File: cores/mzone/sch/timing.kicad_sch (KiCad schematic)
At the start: 39 parts

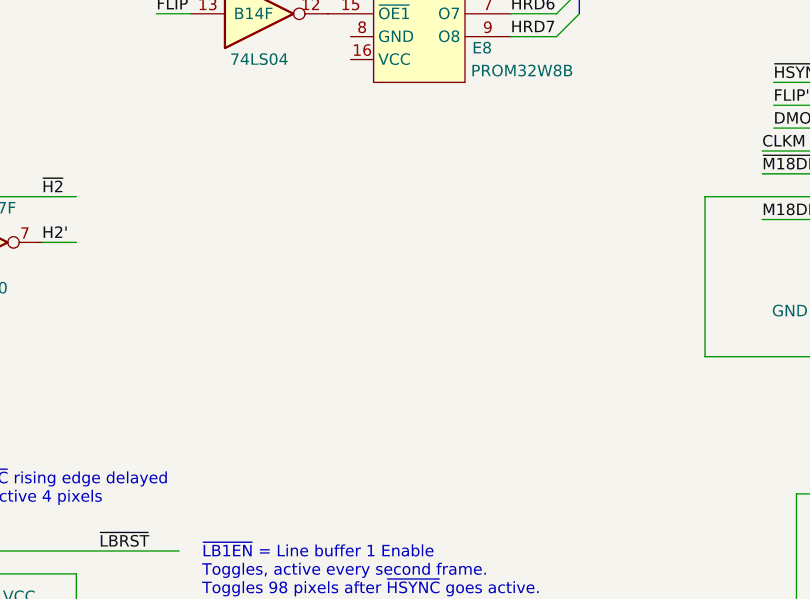
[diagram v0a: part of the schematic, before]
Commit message: mzone core
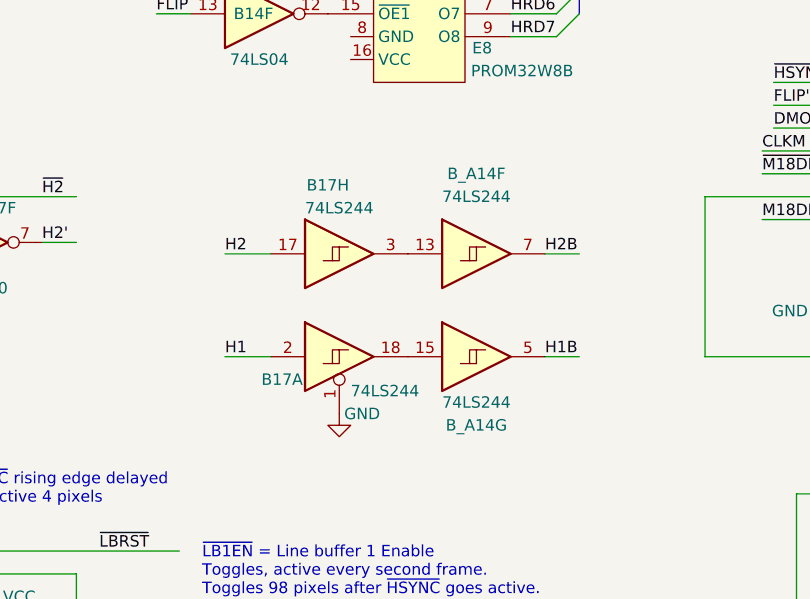
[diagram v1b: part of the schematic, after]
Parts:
- added B17, B_A14: 74LS244, symbol 74xx:74LS244_Split
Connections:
- net GND: now also B17.1
- net H1: now also B17.2
- net H2: now also B17.17
- new net: B17.18, B_A14.15
- new net: B17.3, B_A14.13
- new net H1B: B_A14.5
- new net H2B: B_A14.7

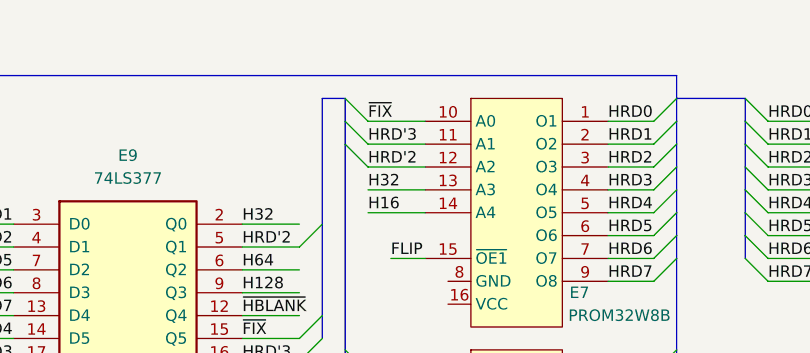
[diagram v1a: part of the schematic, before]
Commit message: mzone core
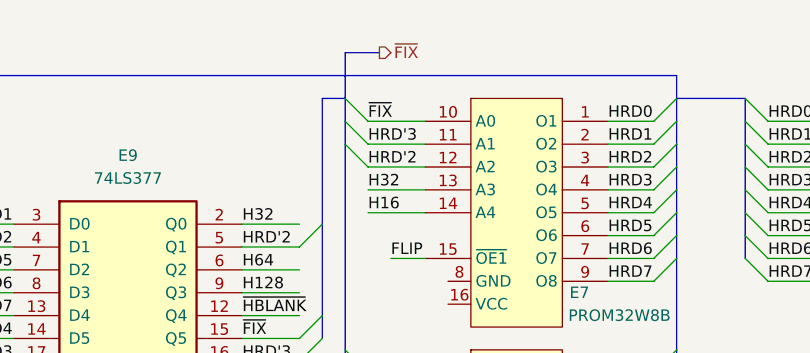
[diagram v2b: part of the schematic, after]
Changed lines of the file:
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@@
 		)
 	)
+	(bus
+		(pts
+			(xy 290.83 22.86) (xy 290.83 17.78)
+		)
+		(stroke
+			(width 0)
+			(type default)
+		)
+	)
 	(wire
 		(pts
@@
 	(bus
 		(pts
+			(xy 290.83 17.78) (xy 294.64 17.78)
+		)
+		(stroke
+			(width 0)
+			(type default)
+		)
+	)
+	(bus
+		(pts
 			(xy 290.83 53.34) (xy 290.83 50.8)
 		)
@@
 	(label "H2"
 		(at 288.29 95.25 0)
-		(fields_autoplaced yes)
 		(effects
 			(font
@@
 	(label "H1B"
 		(at 323.85 106.68 0)
-		(fields_autoplaced yes)
 		(effects
 			(font
@@
 	(label "H2B"
 		(at 323.85 95.25 0)
-		(fields_autoplaced yes)
 		(effects
 			(font
@@
 	(label "H1"
 		(at 288.29 106.68 0)
-		(fields_autoplaced yes)
 		(effects
 			(font
@@
 		(effects
 			(font
+				(size 1.27 1.27)
+			)
+			(justify left)
+		)
+	)
+	(hierarchical_label "~{FIX}"
+		(shape output)
+		(at 294.64 17.78 0)
+		(effects
+			(font

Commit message: mzone core
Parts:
- added unit 7 of G4
- added unit 8 of G4
- added unit 9 of G4
- added unit 3 of G4
- added unit 6 of G4
- added unit 2 of G4
- added unit 4 of G4
- added unit 5 of G4
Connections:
- net GND: now also G4.19
- net ~{M18DIV2}: now also G4.11
- net M18DIV2' renamed ~{OCK}
- net M18DIV4 renamed OC0
- net M18DIV8 renamed OC1
- new net OCK: G4.9
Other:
- note added: "M18DIV16"
- note added: "M18DIV32"
- note added: "M18DIV4"
- note added: "M18DIV8"
- note added: "M18DIV8M4"
- moved on the sheet: G6A

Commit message: mzone core
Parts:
- removed G4: 74LS240, symbol jt74:74LS240
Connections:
- net CLKM is gone; now on net OCK: D7.6
- net CLKM' is gone; now on net OCK': A_D5.3 (I1a)
- net DMOT is gone; now on an unnamed net: A_D14.15 (TC)
- net FLIP': now also G4.4
- net GND: now also G4.1
- net HSYNC76: now also G4.18
- net M18DIV16: now also G4.15
- net OCK: now also G4.8; no longer G4.9
- net ~{DMOT}: now also G4.14
- net ~{FLIP}: now also G4.16
- net ~{HSYNC76}: now also G4.2
- net at C13.1: now also G4.12, G4.13
- net OCK': now reaches G4.7
- net DM0 renamed OA0
- net DM1 renamed OA1
- net DM2 renamed OA2
- net DM3 renamed OA3
- net DM4 renamed OA4
- net DM5 renamed OA5
- net DM6 renamed OA6
- net DM7 renamed OA7
- net OC0 renamed OP0
- net OC1 renamed OP1
- net ~{OCK} renamed ~{OPCK}
- new net OPCK: G4.9
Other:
- note added: "OP1OP0"
- note added: "Object Data Byte"
- note added: "Object Phase counters"
- note removed: "The delay going high is T_LH = 50ohm x 0.47nF = 23.5ns The delay going low is T_HL = 0ns"
- moved on the sheet: A_D14, A_D15, A_D5, B_B14H, B_D14A, C14B, C17H, C40, C43, F6A, F6B, F7A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

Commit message: mzone core
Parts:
- removed E10: 74LS240, symbol jt74:74LS240
- added E10: 74LS240, symbol 74xx:74LS240_Split
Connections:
- net GND: now also B16.2 (GND), E7.8 (GND), E8.8 (GND), G4.10 (GND), E10.1, E10.10 (GND), E10.19; no longer C15.3 (D0), C15.4 (D1), C15.5 (D2), C15.6 (D3)
- net H1: now also E10.11
- net HSYNC: now also E10.12
- net V1: now also B12.9 (~{PE}), B13.9 (~{PE}), B14.2
- net VCC: now also E7.16 (VCC), E8.16 (VCC), G4.20 (VCC), E10.20 (VCC)
- net WRIH: now also E10.5
- net ~{HSYNC}: now also E10.8
- net ~{OP}2: now reaches G4.5
- net CLK1 renamed PXCK1
- net CLK2' renamed PXCK2''
- net DMCNTEN renamed OACNTEN
- net H128 renamed HF128
- net H16 renamed HF16
- net H2F renamed HF2
- net H32 renamed HF32
- net HF32: now also E10.2
- net H4F renamed HF4
- net H64 renamed HF64
- net H8F renamed HF8
- net HSYNC76: no longer names the net of G4.18, G5.2
- net M18: no longer names the net of B16.3 (OUT), C16.12 (C), C16.9 (C), G6.3 (C)
- net M18DIV16 renamed OP2
- net M18DIV32 renamed OP3
- net M18DIV8M4 renamed OP0OP1
- net OCK: no longer names the net of D7.6, G4.8
- net OCK' renamed OACK
- net ~{CLK2} renamed ~{PXCK2}
- net ~{PXCK2}: now also E10.17, E10.4
- net ~{DMCNTEN'} renamed ~{OACNTEN'}
- net ~{DMCNTEN} renamed ~{OACNTEN}
- net ~{DMOT} renamed ~{OAOF}
- net ~{H32}: no longer names the net of B11.1
- net ~{H32}: now also E10.18
- net ~{HSYNC76}: no longer names the net of G2.11 (Q5), G4.2
- net ~{M18DIV2}: no longer names the net of G4.11, G6.5 (Q)
- new net: E10.6, E10.9
- new net: E10.14, E10.15
- new net PXCK2: E10.16
- new net PXCK2': E10.3
- no-connect marks 34 -> 40
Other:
- note added: "Object Counters"
- note added: "Object Line Buffer"
- note added: "PXCK1: f_CLK1 = f_M18 / 3"
- note added: "Pixel clock: 18.432MHz / 3 = 6.144MHz, T = 0.16276us Hsync: Low 32px, High: 352px, Total: 384px, f = 6.144MHz / 384 = 16kHz HBlank: Low 97px (Flipped 96), Front Porch: 32px, Back Porch: 32px, Active pixels: 384 - 97 = 287 (288 flipped)"
- note added: "Vertical Blanking"
- note added: "Vertical Counters"
- note added: "not correct symbol?!"
- note removed: "CLK1: f_CLK1 = f_M18 / 3"
- note removed: "M18DIV16"
- note removed: "M18DIV32"
- note removed: "M18DIV4"
- note removed: "M18DIV8"
- note removed: "M18DIV8M4"
- note removed: "OP1OP0"
- note removed: "Pixel clock: 18.432MHz / 3 = 6.144MHz, T = 0.16276us Hsync: Low 32px, High: 352px, Total: 384px, f = 6.144MHz / 384 = 16kHz HBlank: Low 97px, Front Porch: 32px, Back Porch: 32px, Active pixels: 384 - 97 = 287"
- note removed: "WRIH = H1"
- note removed: "not correct symbol"
- note removed: "not sure GND, check"
- moved on the sheet: A_D14, A_D15, A_D5, B11A, B12, B13, B14A, B14D, B14F, B15B, B17A, B17H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

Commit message: mzone core
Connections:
- net V128F renamed VF128
- net V16F renamed VF16
- net V1F renamed VF1
- net V2F renamed VF2
- net V32F renamed VF32
- net V4F renamed VF4
- net V64F renamed VF64
- net V8F renamed VF8
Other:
- note added: "Clocks"
- note added: "Horizontal Counters"
- note added: "Object Data Timing"
- note added: "Sync"
- moved on the sheet: B11A, B15B, DE18D, E10A, E10D

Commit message: mzone core
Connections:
- net ~{H1}: now reaches E10.6, E10.9
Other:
- note added: "Pixel clock: 18.432MHz / 3 = 6.144MHz, T = 0.16276us Hsync: Low 32px, High: 352px, Total: 384px, f = 6.144MHz / 384 = 16kHz HBlank: Low 97px (Flipped 96), Front Porch: 32px, Back Porch: 32px, Active pixels: 384 - 97 = 287 (288 flipped) Diagram is for non-flipped timing."
- note added: "Timing"
- note added: "~{ODB}[6..0]"
- note removed: "Pixel clock: 18.432MHz / 3 = 6.144MHz, T = 0.16276us Hsync: Low 32px, High: 352px, Total: 384px, f = 6.144MHz / 384 = 16kHz HBlank: Low 97px (Flipped 96), Front Porch: 32px, Back Porch: 32px, Active pixels: 384 - 97 = 287 (288 flipped)"
- moved on the sheet: B11A, B14D, B14F, B15A, B15B, B15C, B15D, B16, B17A, B17H, B_A14F, B_A14G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
